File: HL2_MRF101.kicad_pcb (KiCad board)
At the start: 4 copper layers, 149.9 x 100 mm, 190 parts, among them J1 Antenna, J2 HL2, J3 RF3, J4 RF1, J5 RCJ-041, J6 50VDC, J7 12V, J8 Fan, J9 HL2_12V, K1 EC2-3NU, K10 EC2-3NU, K11 EC2-3NU, K12 EC2-3NU, K13 EC2-3NU, K2 EC2-3NU, K3 EC2-3NU, K4 EC2-3NU, K5 EC2-3NU, K6 EC2-3NU, K7 EC2-3NU, K8 EC2-3NU, K9 EC2-3NU, Q1 MRF101AN, Q2 2N7002, Q3 NSS60601MZ4, T1 Coupler, T2 Coupler, T3 744851330, U1 MCP6282E/MS, U3 MCP23008, U4 ULN2003, U5 LM35-NEB, U6 LM393

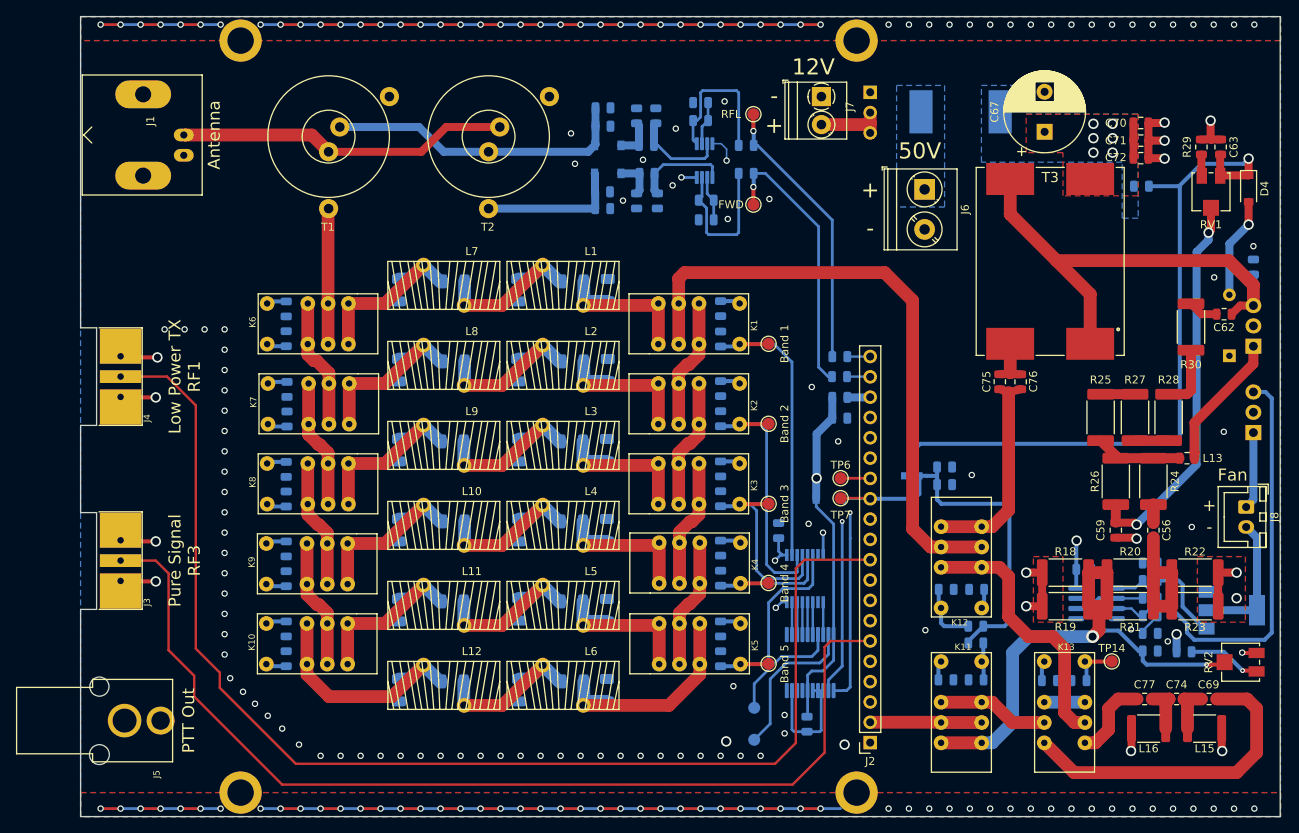
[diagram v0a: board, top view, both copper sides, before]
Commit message: Relocated C47
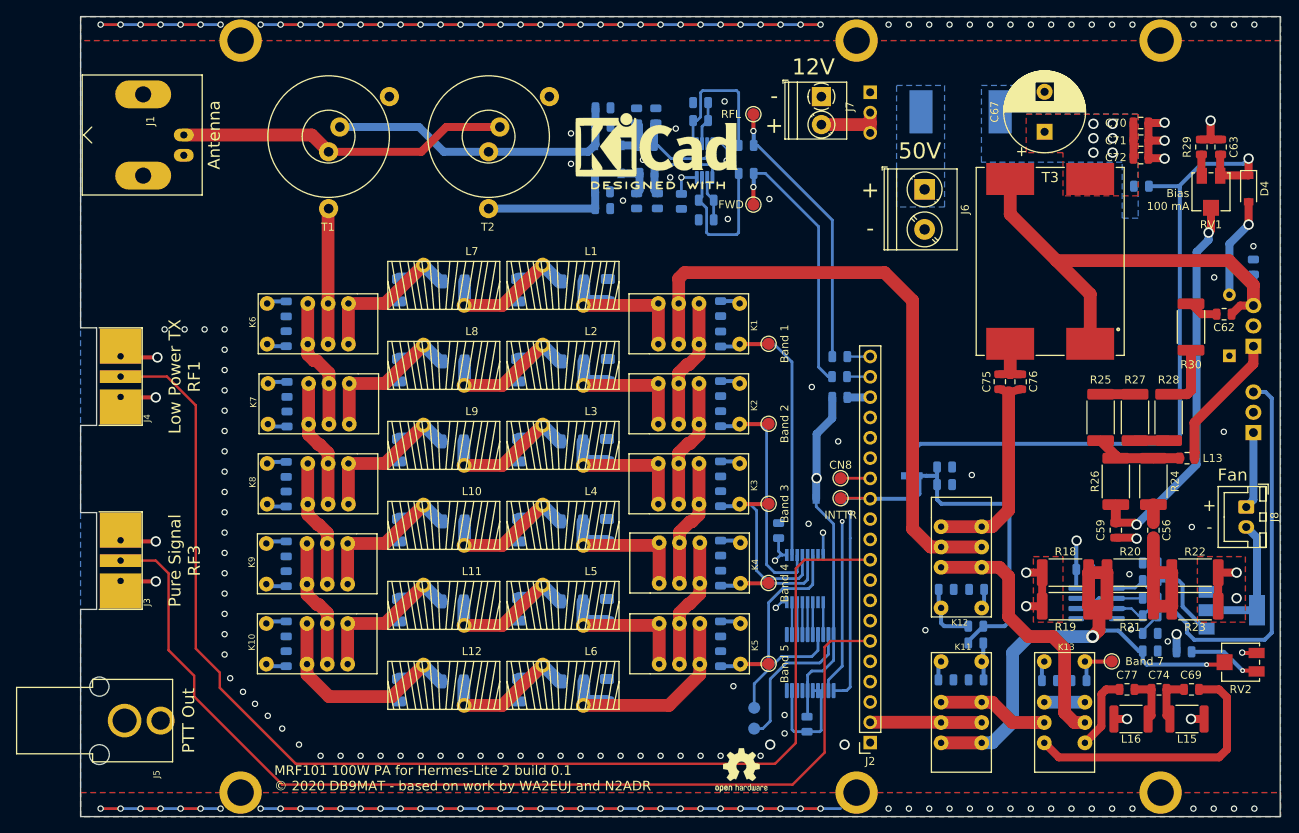
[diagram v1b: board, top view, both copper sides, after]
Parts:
- added REF**: KiCad-Logo2_8mm_SilkScreen, Symbol:KiCad-Logo2_8mm_SilkScreen, F.Cu at (142.0, 56.0)
- added REF**: OSHW-Logo2_7.3x6mm_SilkScreen, Symbol:OSHW-Logo2_7.3x6mm_SilkScreen, B.Cu at (152.6, 134.2)
- added REF**: OSHW-Logo2_7.3x6mm_SilkScreen, Symbol:OSHW-Logo2_7.3x6mm_SilkScreen, F.Cu at (152.6, 134.2)
- added REF**: VAL**, n2adr:m3, F.Cu at (205.0, 137.0)
- added REF**: VAL**, n2adr:m3, F.Cu at (205.0, 43.0)
- Band 7: renamed from TP14
- moved C47 33.6 mm to (145.1, 63.1), turned to 90 degrees
- moved C69 2.51 mm to (208.9, 124.1)
- moved C74 2.51 mm to (204.8, 124.1)
- moved C77 2.51 mm to (200.8, 124.1)
- moved L15 2.51 mm to (208.3, 127.8)
- moved L16 2.51 mm to (201.3, 127.8)
- moved TP4 1.40 mm to (154.2, 129.0)
- renumbered TP6 to CN8, TP7 to INTTR
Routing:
- net Net-(C69-Pad2): track 40.1 -> 34.4 mm
- net +3V3: track 362.7 -> 358.2 mm
- net GND: track 251.0 -> 248.6 mm, vias 200 -> 197
- net Net-(C77-Pad1): track 10.3 -> 9.44 mm
- net Net-(TP4-Pad1): track 19.5 -> 18.7 mm
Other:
- board text added: "Bias 100 mA"
- board text added: "MRF101 100W PA for Hermes-Lite 2 build 0.1 © 2020 DB9MAT - based on work by WA2EUJ and N2ADR"

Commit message: Updated R6-9 to 1206 1/2W
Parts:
- R6, R7, R8, R9: footprint Resistor_SMD:R_0805_2012Metric -> Resistor_SMD:R_1206_3216Metric
- moved R7 0.72 mm to (135.9, 64.4)
- moved R6 0.61 mm to (135.8, 62.0)
- moved R8 0.51 mm to (135.8, 51.3)
- moved R9 0.50 mm to (135.8, 53.7)
